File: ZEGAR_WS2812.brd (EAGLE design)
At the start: 121.4 x 121.4 mm, 151 parts, among them IC2 DS3231/SO, IC3 ATMEGA328P, Q2 MMBT3906LT1SMD, Q3 MMBT3906LT1SMD, Q4 MMBT3906LT1SMD, Q5 MMBT3906LT1SMD, U1 SN74HC595D, U10 SN74HC595D, U2 SN74HC595D, U3 SN74HC595D, U4 SN74HC595D, U5 SN74HC595D, U6 SN74HC595D, U7 SN74HC595D, U8 SN74HC595D, U9 SN74HC595D

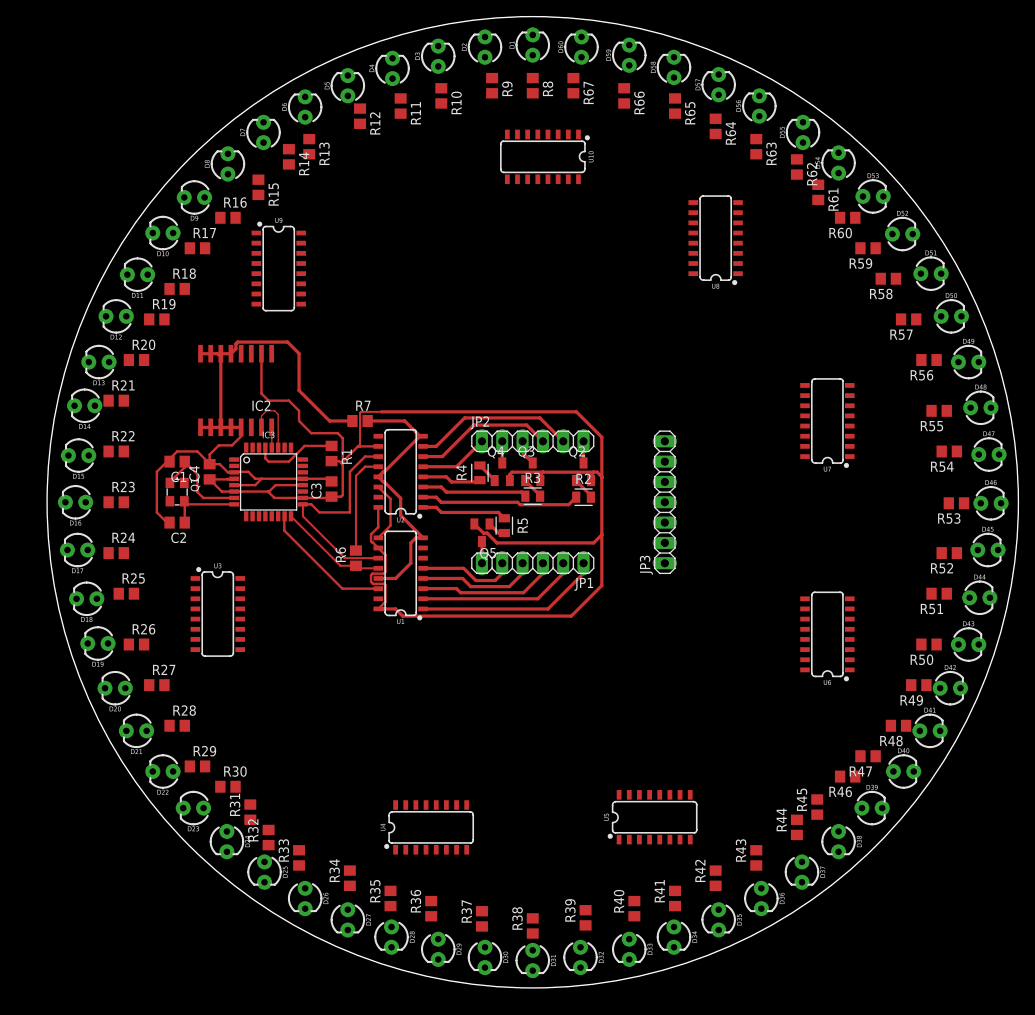
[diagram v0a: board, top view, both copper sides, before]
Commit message: fixed hc595 posiiton
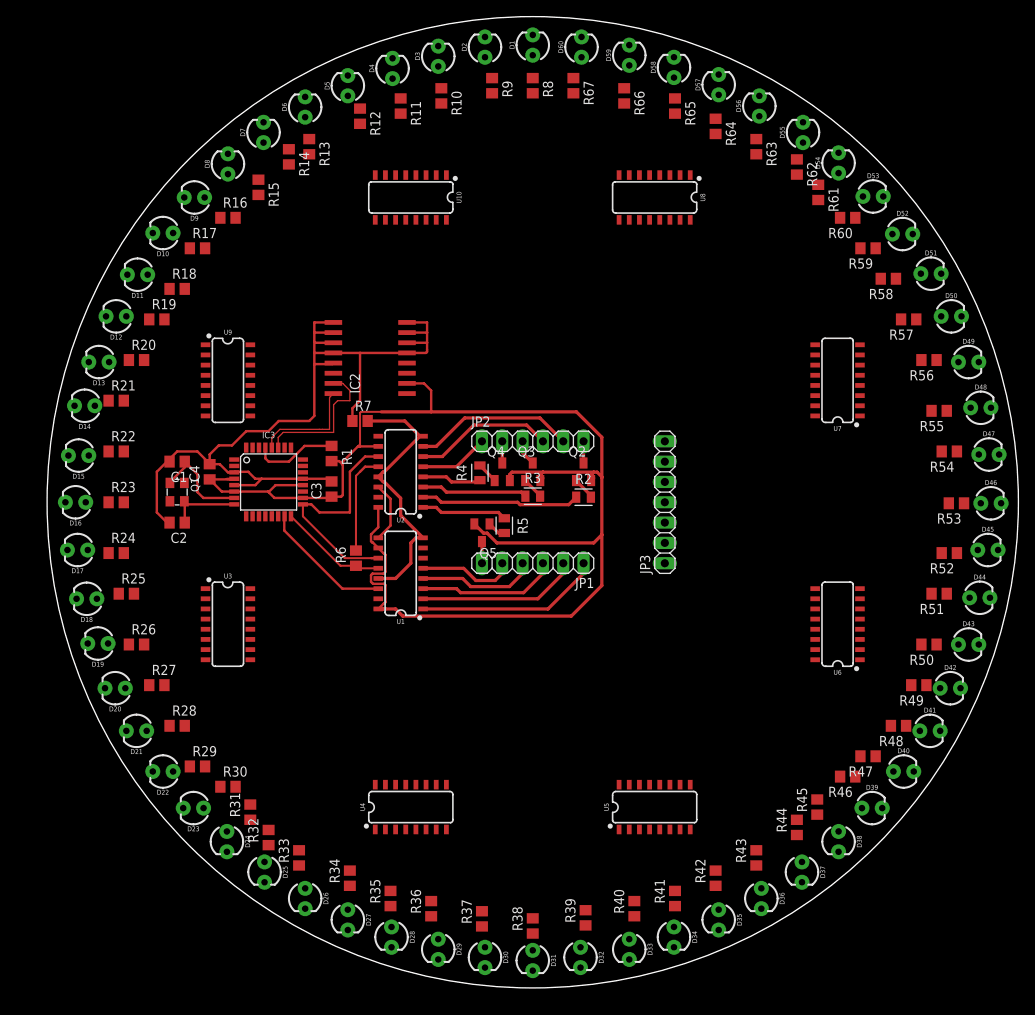
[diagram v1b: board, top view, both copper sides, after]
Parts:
- moved U10 17.3 mm to (-15.2, 38.1)
- moved IC2 17.2 mm to (-20.3, 18.0), turned to 90 degrees
- moved U9 15.3 mm to (-38.1, 15.2)
- moved U8 9.16 mm to (15.2, 38.1), turned to 180 degrees
- moved U7 5.24 mm to (38.1, 15.2)
- moved U4 3.59 mm to (-15.2, -38.1)
- moved U6 1.80 mm to (38.1, -15.2)
- moved U3 1.80 mm to (-38.1, -15.2)
- moved U5 1.27 mm to (15.2, -38.1)
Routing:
- net GND: track 118.3 -> 141.8 mm
- net 5VCC: track 195.3 -> 180.3 mm
- net SCL: track 2.55 -> 13.6 mm
- net SDA: track 8.12 -> 17.9 mm

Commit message: placed traces from diodes to shift registers
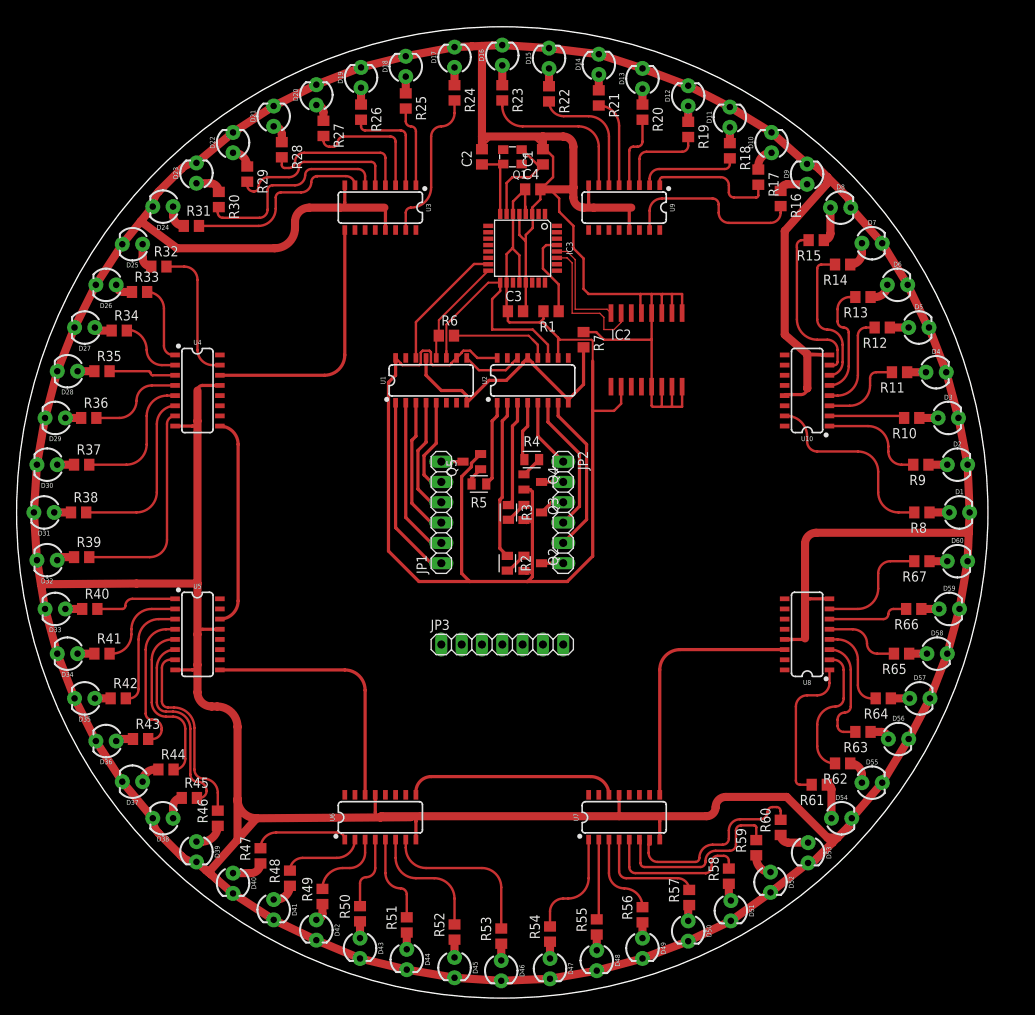
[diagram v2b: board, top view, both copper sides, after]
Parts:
- moved D41 85.0 mm to (-32.4, -50.9), turned to 270 degrees
- moved D43 85.0 mm to (-21.6, -55.8), turned to 270 degrees
- moved D40 85.0 mm to (-37.5, -47.6), turned to 270 degrees
- moved D42 84.8 mm to (-27.1, -53.5), turned to 270 degrees
- moved D44 84.7 mm to (-15.7, -57.1), turned to 270 degrees
- moved D45 84.7 mm to (-9.78, -58.2), turned to 270 degrees
- moved D39 84.6 mm to (-42.0, -43.7), turned to 270 degrees
- moved D46 84.6 mm to (-3.94, -58.5), turned to 270 degrees
- moved D38 84.5 mm to (-46.2, -39.5), turned to 180 degrees
- moved D47 84.5 mm to (2.16, -58.3), turned to 270 degrees
- moved D37 84.5 mm to (-50.0, -34.9), turned to 180 degrees
- moved D36 84.2 mm to (-53.3, -29.8), turned to 180 degrees
- moved D48 84.1 mm to (8.00, -57.3), turned to 270 degrees
- moved D35 83.9 mm to (-56.0, -24.5), turned to 180 degrees
- moved D49 83.9 mm to (13.7, -55.8), turned to 270 degrees
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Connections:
- net 5VCC: now also U10.10
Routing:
- net GND: track 141.8 -> 876.9 mm
- net N$14: track 0.00 -> 32.3 mm
- net N$12: track 0.00 -> 32.3 mm
- net N$10: track 0.00 -> 32.3 mm
- net N$44: track 0.00 -> 26.5 mm
- net N$11: track 0.00 -> 26.2 mm
- net N$13: track 0.00 -> 26.0 mm
- net N$35: track 0.00 -> 24.9 mm
- net N$65: track 0.00 -> 23.8 mm
- net N$36: track 0.00 -> 23.5 mm
- net N$51: track 0.00 -> 23.3 mm
- net N$52: track 0.00 -> 23.3 mm
- net N$4: track 0.00 -> 23.1 mm
- net N$17: track 0.00 -> 22.6 mm
- net N$64: track 0.00 -> 22.6 mm
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
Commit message: hc595 for seconds completed
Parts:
- removed JP3: (no value), pinhead:1X07
- added C10, C11, C12, C5, C6, C7, C8, C9: 100n, rcl:C0805
- added R68, R72, R77, R78, R79, R80, R81: 0, rcl:R2512
- added R69, R70, R71, R73, R74, R75, R76: 0, rcl:R1206
- moved U2 26.1 mm to (-19.1, -2.54), turned to 90 degrees
- moved JP1 13.1 mm to (0.00, -7.62), turned to 180 degrees
- moved Q2 13.1 mm to (6.35, 3.81), turned to 0 degrees
- moved R2 12.0 mm to (2.92, 2.67), turned to 0 degrees
- moved JP2 9.67 mm to (0.00, 7.62), turned to 0 degrees
- moved Q5 8.98 mm to (-6.35, -3.81), turned to 180 degrees
- moved R6 8.13 mm to (-5.71, 27.2)
- moved R4 7.00 mm to (-6.86, 3.43), turned to 270 degrees
- moved U1 6.48 mm to (-19.1, 14.0), turned to 90 degrees
- moved R5 6.17 mm to (-3.05, -2.67)
- moved Q3 5.11 mm to (-0.51, 3.81), turned to 0 degrees
- moved Q4 4.38 mm to (-4.19, 3.81), turned to 0 degrees
- moved D10 4.02 mm to (33.7, 46.2)
- moved D19 4.02 mm to (-17.7, 54.4)
- moved D22 4.02 mm to (-33.7, 46.2)
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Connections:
- removed net N$3: U3.14, U9.9
- new net N$133: U9.9
- new net SEC_SER: U3.14
- net 4DIG_1IN: now also U1.2; no longer U2.2
- net 4DIG_2IN: now also U1.3; no longer U2.3
- net 4DIG_3IN: now also U1.4; no longer U2.4
- net 4DIG_4IN: now also U1.1; no longer U2.1
- net 4DIG_A: now also U1.7; no longer U2.7
- net 4DIG_B: now also U1.5; no longer U2.5
- net 4DIG_C: now also U2.6; no longer U1.4
- net 4DIG_D: now also U2.4; no longer U1.2
- net 4DIG_DP: now also U2.5; no longer U1.3
- net 4DIG_E: now also U2.3; no longer U1.1
- net 4DIG_F: now also U1.6; no longer U2.6
- net 4DIG_G: now also U2.7; no longer U1.5
- net 5VCC: now also C10.2, C11.2, C12.2, C5.1, C6.1, C7.1, C8.1, C9.1, R68.1, R68.2, R72.1, R72.2, R77.1, R77.2, R78.1, R78.2, R79.1, R79.2, R80.1, R80.2, R81.1, R81.2
- net GND: now also C10.1, C11.1, C12.1, C5.2, C6.2, C7.2, C8.2, C9.2
- net SEC_CLK: now also R69.1, R69.2, R70.1, R70.2, R71.1, R71.2, R73.1, R73.2, R74.1, R74.2
- net SEC_LATCH: now also R75.1, R75.2, R76.1, R76.2
- net SEC_SERIAL: now also U8.9
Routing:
- net 5VCC: track 180.3 -> 582.6 mm
- net SEC_LATCH: track 0.00 -> 247.2 mm
- net SEC_CLK: track 0.00 -> 245.2 mm
- net SEC_SERIAL: track 0.00 -> 31.9 mm
- net 4DIG_CLK: track 29.7 -> 0.00 mm
- net N$2: track 0.00 -> 29.3 mm
- net 4DIG_LATCH: track 26.2 -> 0.45 mm
- net 4DIG_SER: track 16.6 -> 0.14 mm
- net 4DIG_4IN: track 10.7 -> 22.6 mm
- net GND: track 876.9 -> 888.5 mm
- net 4DIG_1IN: track 19.9 -> 29.4 mm
- net 4DIG_E: track 23.2 -> 32.5 mm
- net 4DIG_A: track 20.2 -> 29.4 mm
- net 4DIG_D: track 20.1 -> 29.1 mm
- net 4DIG_2IN: track 13.3 -> 22.3 mm
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
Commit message: almost done
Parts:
- removed R7: 0, rcl:R0805
- added R82, R83, R87: 0, rcl:R2512
- added R84, R85, R86, R88: 1k, Resistor:RESC2012X65
- added S1, S2, S3, S4: (no value), switch-omron:B3F-10XX
- added U$1: TP4056-PTH, 32teeth - TP4056 Module:TP4056-PTH
- R6: device rcl:R0805 -> rcl:R2512
- moved R6 25.9 mm to (-31.4, 23.5), turned to 180 degrees
- moved R68 5.22 mm to (-10.8, 30.5), turned to 90 degrees
- moved R74 0.64 mm to (-31.8, 14.6)
- moved R1 0.38 mm to (5.71, 25.1)
- moved C3 0.13 mm to (1.52, 25.1)
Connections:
- new net BUTTONS: IC3.25, R84.2, R87.1, R87.2, R88.1, S1.3, S1.4
- new net N$138: R84.1, R85.2, S2.3, S2.4
- new net N$139: R85.1, R86.2, S3.3, S3.4
- new net N$140: R86.1, S4.3, S4.4
- net 4DIG_CLK: now also IC3.13; no longer IC3.17
- net 4DIG_LATCH: now also IC3.12, R83.1, R83.2; no longer IC3.16, R6.1, R6.2
- net 4DIG_SER: now also IC3.14; no longer IC3.15
- net 5VCC: now also R6.1, R6.2, R82.1, R82.2, R88.2
- net GND: now also S1.1, S1.2, S2.1, S2.2, S3.1, S3.2, S4.1, S4.2; no longer R7.1, R7.2
- net SEC_CLK: now also IC3.10
- net SEC_LATCH: now also IC3.11
- net SEC_SER: now also IC3.9
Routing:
- net 5VCC: track 582.6 -> 784.6 mm
- net GND: track 888.5 -> 1042.7 mm
- net BUTTONS: track 0.00 -> 74.2 mm
- net 4DIG_CLK: track 0.00 -> 55.2 mm
- net 4DIG_LATCH: track 0.45 -> 55.4 mm
- net 4DIG_SER: track 0.14 -> 36.9 mm
- net N$1: track 0.00 -> 31.8 mm
- net SEC_CLK: track 245.2 -> 268.0 mm
- net N$138: track 0.00 -> 19.7 mm
- net N$139: track 0.00 -> 19.4 mm
- net SEC_SER: track 0.00 -> 18.3 mm
- net SEC_LATCH: track 247.2 -> 264.0 mm
- net N$140: track 0.00 -> 16.5 mm
- net N$64: track 22.6 -> 20.9 mm
- net N$65: track 23.8 -> 22.4 mm
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
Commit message: done?
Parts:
- removed U$1: TP4056-PTH, 32teeth - TP4056 Module:TP4056-PTH
- added JP3: (no value), pinhead-2:2X03SMD
- added R7: 0, rcl:R1206
- moved C12 2.29 mm to (11.3, 33.1)
- moved R3 0.28 mm to (-2.29, 0.76)
- moved R87 0.13 mm to (10.4, 20.2)
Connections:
- new net MISO: IC3.16, JP3.1
- new net MOSI: IC3.15, JP3.4
- new net SCK: IC3.17, JP3.3
- net 5VCC: now also JP3.2
- net GND: now also JP3.6, R7.1, R7.2
- net RESET: now also JP3.5
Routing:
- net SCK: track 0.00 -> 24.5 mm
- net 5VCC: track 784.6 -> 801.9 mm
- net MOSI: track 0.00 -> 15.6 mm
- net GND: track 1042.7 -> 1057.6 mm
- net MISO: track 0.00 -> 8.54 mm
- net 4DIG_A: track 29.4 -> 25.3 mm
- net 4DIG_F: track 24.3 -> 20.9 mm
- net 4DIG_B: track 15.4 -> 13.2 mm
- net SDA: track 16.5 -> 15.5 mm
- net SCL: track 12.5 -> 11.7 mm
- net N$58: track 20.1 -> 19.4 mm
- net 4DIG_2IN: track 22.3 -> 21.6 mm
- net 4DIG_3IN: track 15.7 -> 15.2 mm
- added copper zone on layer 1, net GND

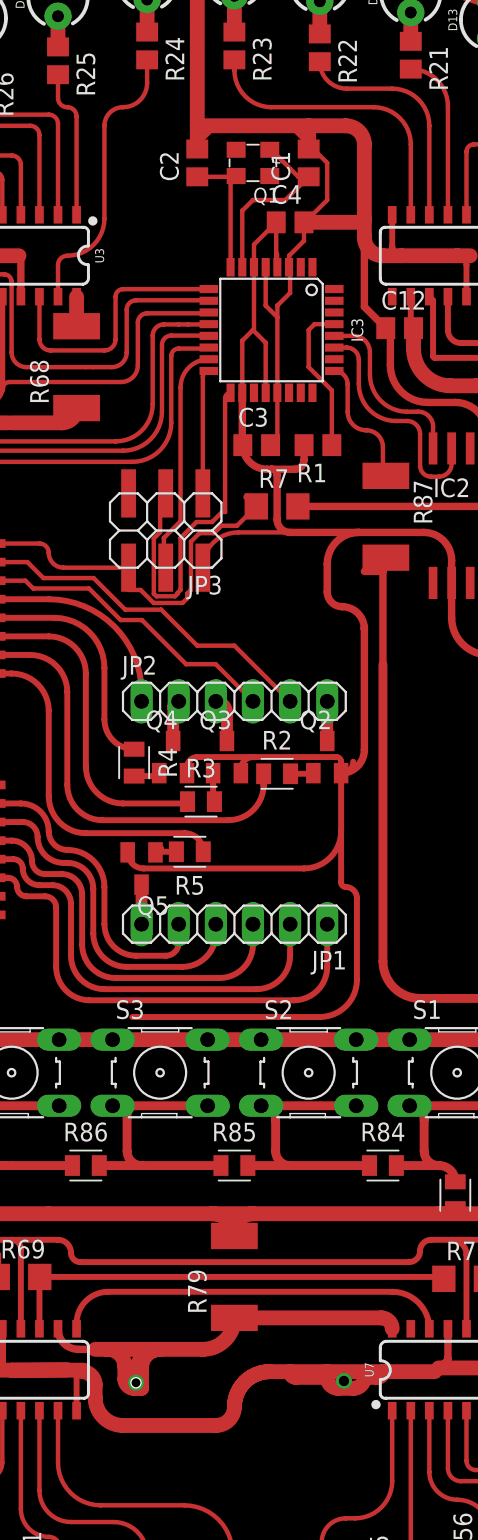
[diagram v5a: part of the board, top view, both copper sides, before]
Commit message: added programming pins and rx tx pins
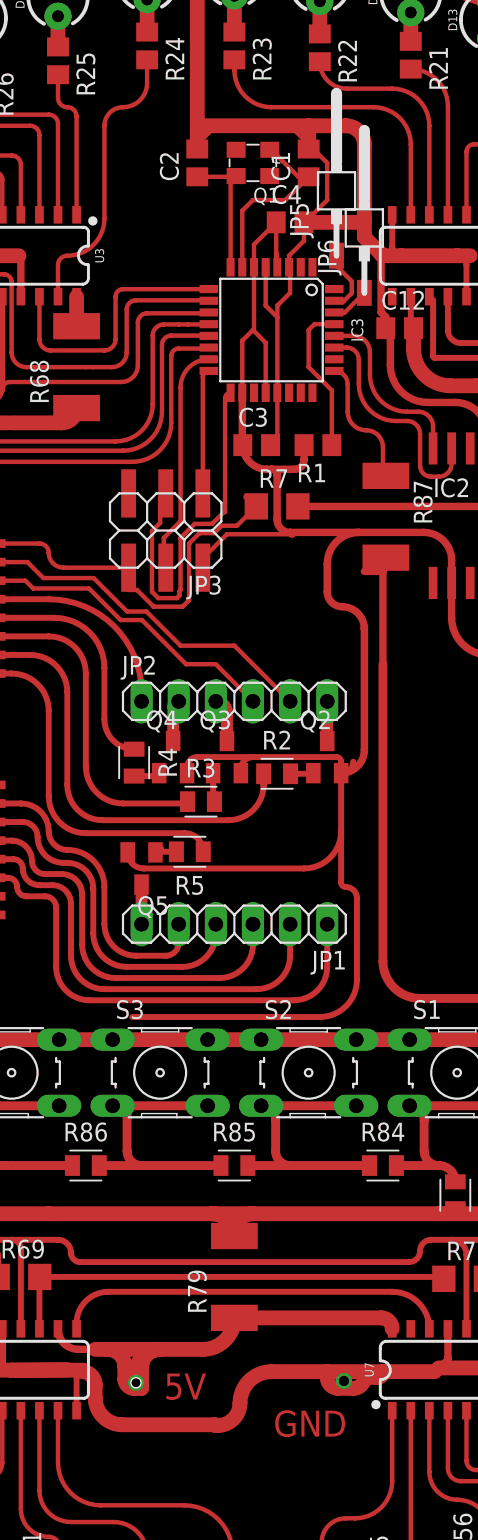
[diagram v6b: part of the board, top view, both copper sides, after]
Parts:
- added JP5, JP6: (no value), pinhead-2:1X01SMD/90
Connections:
- new net N$135: IC3.30, JP6.1
- new net N$136: IC3.31, JP5.1
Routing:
- net GND: track 1057.6 -> 1049.6 mm
- net N$136: track 0.00 -> 4.43 mm
- net N$135: track 0.00 -> 2.61 mm
- net 5VCC: track 801.9 -> 802.5 mm
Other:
- board text added: "5V"
- board text added: "GND"

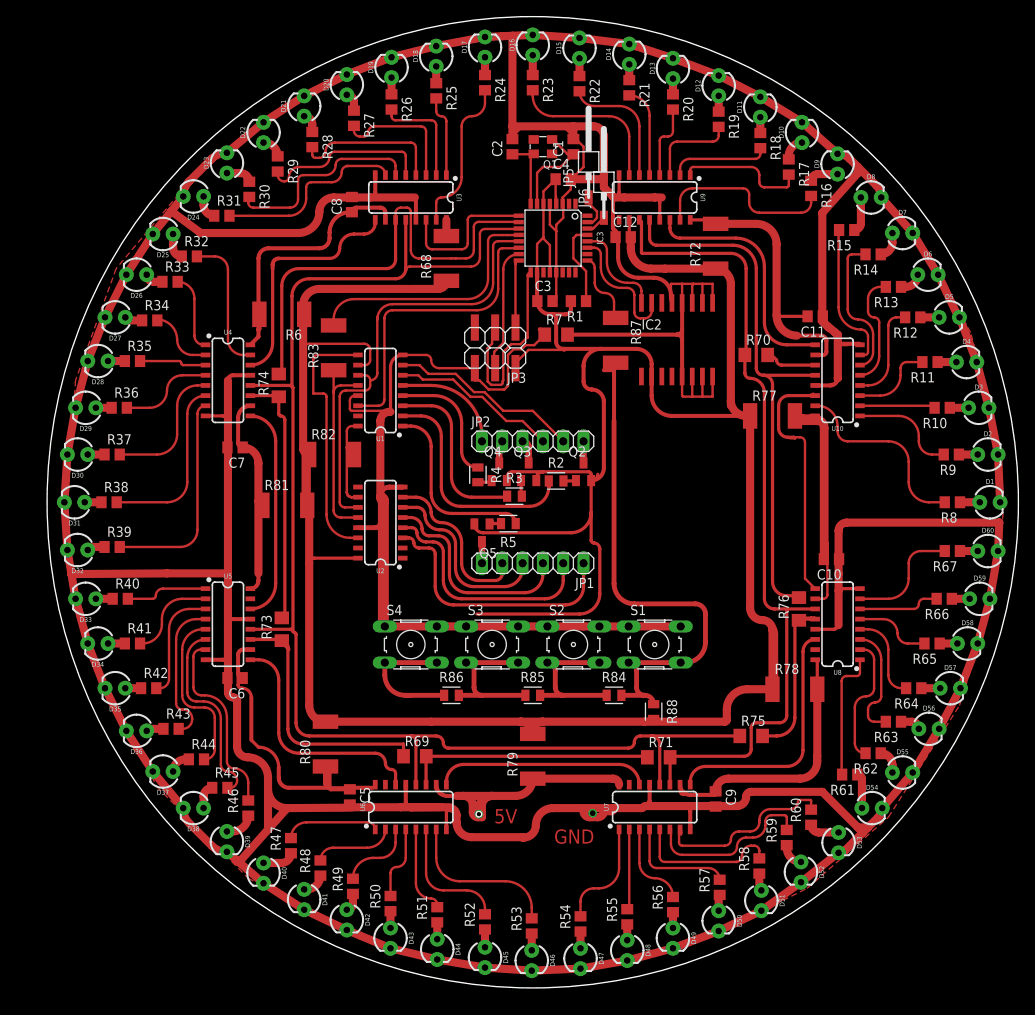
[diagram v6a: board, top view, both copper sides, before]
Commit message: adjusted some traces
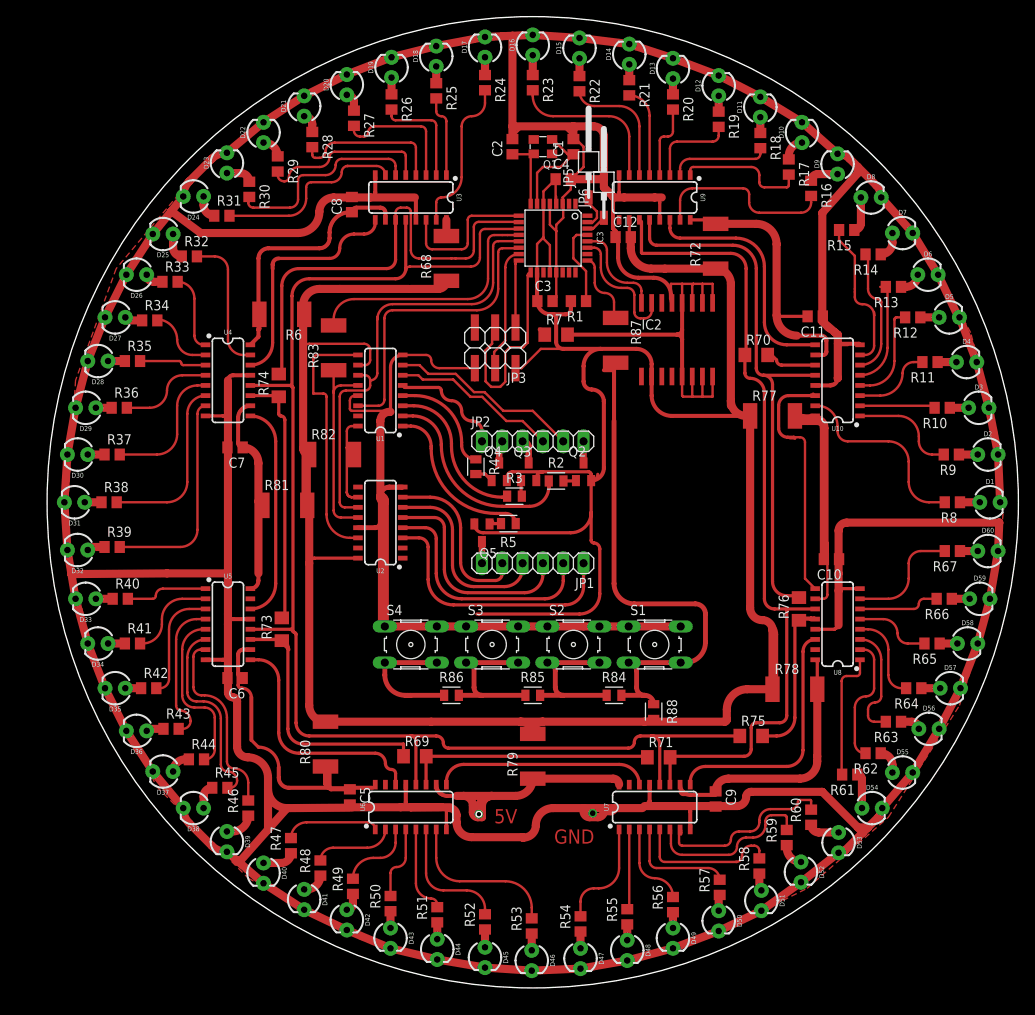
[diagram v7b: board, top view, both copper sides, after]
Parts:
- moved R4 1.05 mm to (-7.11, 4.45)
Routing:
- net GND: track 1049.6 -> 1035.3 mm
- net 4DIG_1IN: track 29.3 -> 25.6 mm
- net 4DIG_2IN: track 21.6 -> 18.1 mm
- net 4DIG_4IN: track 22.6 -> 19.3 mm
- net 4DIG_3IN: track 15.2 -> 12.6 mm
- net N$15: track 17.8 -> 15.8 mm
- net 4DIG_G: track 19.9 -> 20.9 mm
- net 4DIG_DP: track 25.8 -> 26.8 mm
- net N$16: track 18.0 -> 19.0 mm
- net SCK: track 24.9 -> 25.8 mm
- net 4DIG_C: track 22.5 -> 23.3 mm
- net N$9: track 14.0 -> 13.3 mm
- net 5VCC: track 802.5 -> 801.9 mm
- net N$7: track 10.1 -> 9.54 mm
- net N$20: track 1.80 -> 2.31 mm
